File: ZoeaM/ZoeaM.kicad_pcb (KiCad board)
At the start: 2 copper layers, 99.6 x 57.7 mm, 8 parts, among them P1 DummyPad, P2 DummyPad

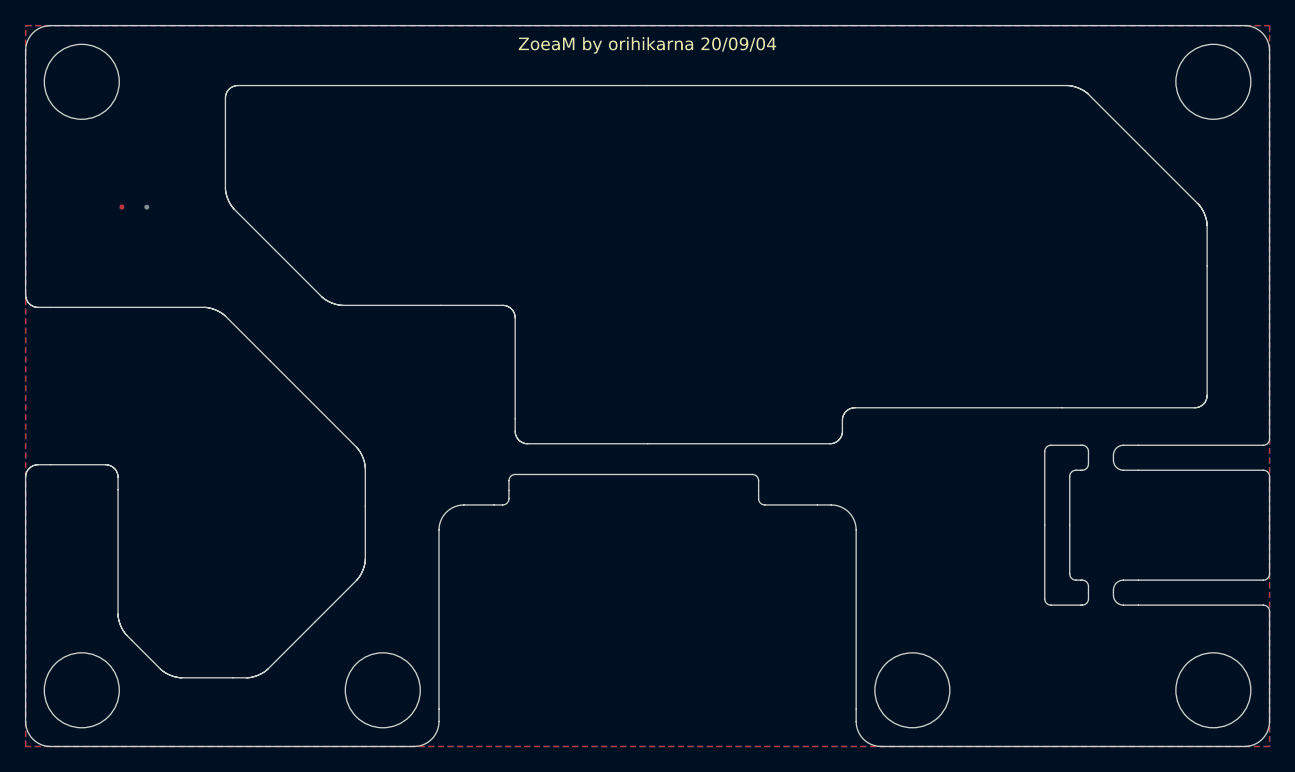
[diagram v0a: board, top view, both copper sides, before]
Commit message: changed mid plate holes to edge.cuts for jlcpcb issue
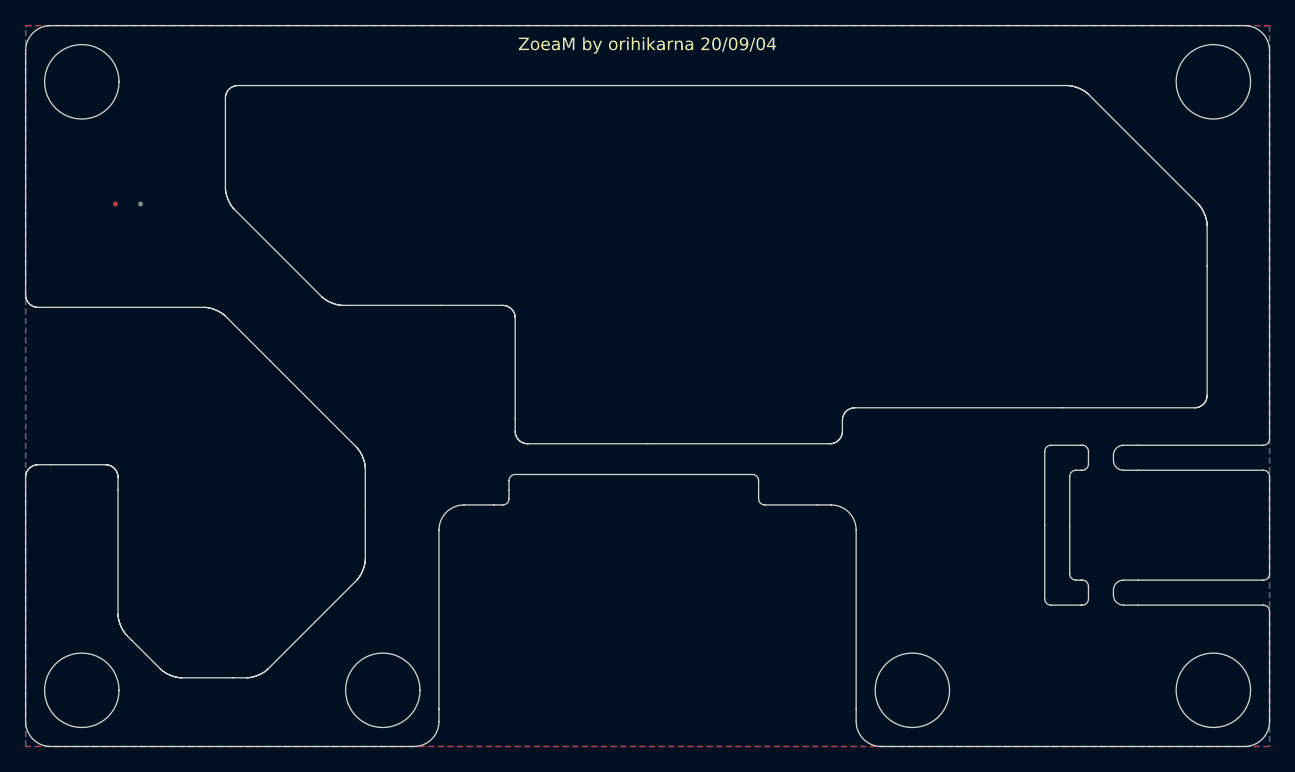
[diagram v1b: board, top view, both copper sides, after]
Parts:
- removed H1, H2, H3, H4, H5, H6: MountingHole, key-parts:MountingHole_6.0mm_M3_Standoff
- moved P2 0.57 mm to (9.20, 14.3)
- moved P1 0.57 mm to (7.20, 14.3)
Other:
- outline, holes or cut-outs redrawn
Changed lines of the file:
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@@
     (tracks 0)
     (zones 0)
-    (modules 8)
+    (modules 2)
     (nets 2)
   )
@@
     (47 F.CrtYd user)
     (48 B.Fab user)
-    (49 F.Fab user)
+    (49 F.Fab user hide)
   )
   (setup
@@
     (visible_elements FFFFFF7F)
     (pcbplotparams
-      (layerselection 0x010f0_ffffffff)
+      (layerselection 0x010e0_ffffffff)
       (usegerberextensions false)
       (usegerberattributes false)
@@
     (add_net GND)
   )
-  (module key-parts:MountingHole_6.0mm_M3_Standoff (layer F.Cu)
-    (at 71 53.22)
-    (descr "Mounting Hole 3.2mm, no annular, M3")
-    (tags "mounting hole 3.2mm no annular m3")
-    (attr virtual)
-    (fp_text reference H6 (at 0 -4.2) (layer F.SilkS) hide
-      (effects (font (size 1 1) (thickness 0.15)))
-    )
-    (fp_text value MountingHole (at 0 4.2) (layer F.Fab) hide
-      (effects (font (size 1 1) (thickness 0.15)))
-    )
-    (fp_circle (center 0 0) (end 3 0) (layer F.CrtYd) (width 0.1))
-    (fp_text user %R (at 0.3 0) (layer F.Fab)
-      (effects (font (size 1 1) (thickness 0.15)))
-    )
-    (pad "" np_thru_hole circle (at 0 0) (size 6 6) (drill 6) (layers *.Cu *.Mask))
-  )
-  (module key-parts:MountingHole_6.0mm_M3_Standoff (layer F.Cu)
-    (at 28.6 53.22)
-    (descr "Mounting Hole 3.2mm, no annular, M3")
-    (tags "mounting hole 3.2mm no annular m3")
-    (attr virtual)
-    (fp_text reference H5 (at 0 -4.2) (layer F.SilkS) hide
-      (effects (font (size 1 1) (thickness 0.15)))
-    )
-    (fp_text value MountingHole (at 0 4.2) (layer F.Fab) hide
-      (effects (font (size 1 1) (thickness 0.15)))
-    )
-    (fp_circle (center 0 0) (end 3 0) (layer F.CrtYd) (width 0.1))
-    (fp_text user %R (at 0.3 0) (layer F.Fab)
-      (effects (font (size 1 1) (thickness 0.15)))
-    )
-    (pad "" np_thru_hole circle (at 0 0) (size 6 6) (drill 6) (layers *.Cu *.Mask))
-  )
-  (module key-parts:MountingHole_6.0mm_M3_Standoff (layer F.Cu)
-    (at 4.5 53.22)
-    (descr "Mounting Hole 3.2mm, no annular, M3")
-    (tags "mounting hole 3.2mm no annular m3")
-    (attr virtual)
-    (fp_text reference H4 (at 0 -4.2) (layer F.SilkS) hide
-      (effects (font (size 1 1) (thickness 0.15)))
-    )
-    (fp_text value MountingHole (at 0 4.2) (layer F.Fab) hide
-      (effects (font (size 1 1) (thickness 0.15)))
-    )
-    (fp_circle (center 0 0) (end 3 0) (layer F.CrtYd) (width 0.1))
-    (fp_text user %R (at 0.3 0) (layer F.Fab)
-      (effects (font (size 1 1) (thickness 0.15)))
-    )
-    (pad "" np_thru_hole circle (at 0 0) (size 6 6) (drill 6) (layers *.Cu *.Mask))
-  )
-  (module key-parts:MountingHole_6.0mm_M3_Standoff (layer F.Cu)
-    (at 95.1 53.22)
-    (descr "Mounting Hole 3.2mm, no annular, M3")
-    (tags "mounting hole 3.2mm no annular m3")
-    (attr virtual)
-    (fp_text reference H3 (at 0 -4.2) (layer F.SilkS) hide
-      (effects (font (size 1 1) (thickness 0.15)))
-    )
-    (fp_text value MountingHole (at 0 4.2) (layer F.Fab) hide
-      (effects (font (size 1 1) (thickness 0.15)))
-    )
-    (fp_circle (center 0 0) (end 3 0) (layer F.CrtYd) (width 0.1))
-    (fp_text user %R (at 0.3 0) (layer F.Fab)
-      (effects (font (size 1 1) (thickness 0.15)))
-    )
-    (pad "" np_thru_hole circle (at 0 0) (size 6 6) (drill 6) (layers *.Cu *.Mask))
-  )
-  (module key-parts:MountingHole_6.0mm_M3_Standoff (layer F.Cu)
-    (at 95.1 4.5)
-    (descr "Mounting Hole 3.2mm, no annular, M3")
-    (tags "mounting hole 3.2mm no annular m3")
-    (attr virtual)
-    (fp_text reference H2 (at 0 -4.2) (layer F.SilkS) hide
-      (effects (font (size 1 1) (thickness 0.15)))
-    )
-    (fp_text value MountingHole (at 0 4.2) (layer F.Fab) hide
-      (effects (font (size 1 1) (thickness 0.15)))
-    )
-    (fp_circle (center 0 0) (end 3 0) (layer F.CrtYd) (width 0.1))
-    (fp_text user %R (at 0.3 0) (layer F.Fab)
-      (effects (font (size 1 1) (thickness 0.15)))
-    )
-    (pad "" np_thru_hole circle (at 0 0) (size 6 6) (drill 6) (layers *.Cu *.Mask))
-  )
-  (module key-parts:MountingHole_6.0mm_M3_Standoff (layer F.Cu)
-    (at 4.5 4.5)
-    (descr "Mounting Hole 3.2mm, no annular, M3")
-    (tags "mounting hole 3.2mm no annular m3")
-    (attr virtual)
-    (fp_text reference H1 (at 0 -4.2) (layer F.SilkS) hide
-      (effects (font (size 1 1) (thickness 0.15)))
-    )
-    (fp_text value MountingHole (at 0 4.2) (layer F.Fab) hide
-      (effects (font (size 1 1) (thickness 0.15)))
-    )
-    (fp_circle (center 0 0) (end 3 0) (layer F.CrtYd) (width 0.1))
-    (fp_text user %R (at 0.3 0) (layer F.Fab)
-      (effects (font (size 1 1) (thickness 0.15)))
-    )
-    (pad "" np_thru_hole circle (at 0 0) (size 6 6) (drill 6) (layers *.Cu *.Mask))
-  )
   (module key-parts:DummyPad (layer B.Cu)
-    (at 9.704999 14.534999)
+    (at 9.196999 14.280999)
     (fp_text reference P2 (at 0 1.5) (layer B.SilkS) hide
       (effects (font (size 1 1) (thickness 0.15)) (justify mirror))
@@
   )
   (module key-parts:DummyPad (layer F.Cu)
-    (at 7.704999 14.534999)
+    (at 7.196999 14.280999)
     (fp_text reference P1 (at 0 -1.5) (layer F.SilkS) hide
       (effects (font (size 1 1) (thickness 0.15)))
@@
       (net 1 GND) (zone_connect 2))
   )
-  (gr_arc (start 71 53.22) (end 74 53.22) (angle 360) (layer F.Fab) (width 0.1))
-  (gr_arc (start 28.6 53.22) (end 31.6 53.22) (angle 360) (layer F.Fab) (width 0.1))
-  (gr_arc (start 4.5 53.22) (end 7.5 53.22) (angle 360) (layer F.Fab) (width 0.1))
-  (gr_arc (start 95.1 53.22) (end 98.1 53.22) (angle 360) (layer F.Fab) (width 0.1))
-  (gr_arc (start 95.1 4.5) (end 98.1 4.5) (angle 360) (layer F.Fab) (width 0.1))
-  (gr_arc (start 4.5 4.5) (end 7.5 4.5) (angle 360) (layer F.Fab) (width 0.1))
+  (gr_arc (start 71 53.22) (end 73.98 53.22) (angle 360) (layer Edge.Cuts) (width 0.1))
+  (gr_arc (start 28.6 53.22) (end 31.58 53.22) (angle 360) (layer Edge.Cuts) (width 0.1))
+  (gr_arc (start 4.5 53.22) (end 7.48 53.22) (angle 360) (layer Edge.Cuts) (width 0.1))
+  (gr_arc (start 95.1 53.22) (end 98.08 53.22) (angle 360) (layer Edge.Cuts) (width 0.1))
+  (gr_arc (start 95.1 4.5) (end 98.08 4.5) (angle 360) (layer Edge.Cuts) (width 0.1))
+  (gr_arc (start 4.5 4.5) (end 7.48 4.5) (angle 360) (layer Edge.Cuts) (width 0.1))
   (gr_line (start 16 13) (end 16 9.62) (layer Edge.Cuts) (width 0.1))
   (gr_line (start 16.001 13.056) (end 16 13) (layer Edge.Cuts) (width 0.1))
@@
   (gr_arc (start 97.6 55.72) (end 99.6 55.72) (angle 90) (layer Edge.Cuts) (width 0.1))
   (gr_line (start 83 57.72) (end 97.6 57.72) (layer Edge.Cuts) (width 0.1))
-  (gr_line (start 99.6 52.72) (end 99.6 55.72) (layer Edge.Cuts) (width 0.1))
+  (gr_line (start 99.6 54.72) (end 99.6 55.72) (layer Edge.Cuts) (width 0.1))
   (gr_arc (start 99.1 46.9) (end 99.1 46.4) (angle 90) (layer Edge.Cuts) (width 0.1))
-  (gr_line (start 99.6 52.72) (end 99.6 46.9) (layer Edge.Cuts) (width 0.1))
+  (gr_line (start 99.6 54.72) (end 99.6 46.9) (layer Edge.Cuts) (width 0.1))
   (gr_line (start 89.1 46.4) (end 99.1 46.4) (layer Edge.Cuts) (width 0.1))
   (gr_arc (start 87.9 45.6) (end 87.9 46.4) (angle 90) (layer Edge.Cuts) (width 0.1))
